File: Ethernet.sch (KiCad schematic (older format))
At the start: 31 parts, among them J1 Wuerth_7499010121A, U3 DP83848C, Y3 25MHz

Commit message: Fix footprints
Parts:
- U3: footprint Package_QFP:LQFP-48_7x7mm_P0.5mm -> Package_QFP:LQFP-48-1EP_7x7mm_P0.5mm_EP3.6x3.6mm
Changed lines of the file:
@@
 F 0 "U3" H 7750 4550 50  0000 C CNN
 F 1 "DP83848C" H 7800 4400 50  0000 C CNN
-F 2 "Package_QFP:LQFP-48_7x7mm_P0.5mm" H 9200 1250 50  0001 C CIN
+F 2 "Package_QFP:LQFP-48-1EP_7x7mm_P0.5mm_EP3.6x3.6mm" H 9200 1250 50  0001 C CIN
 F 3 "http://www.ti.com/lit/ds/symlink/dp83848c.pdf" H 8200 2800 50  0001 C CNN
 	1    8200 2800

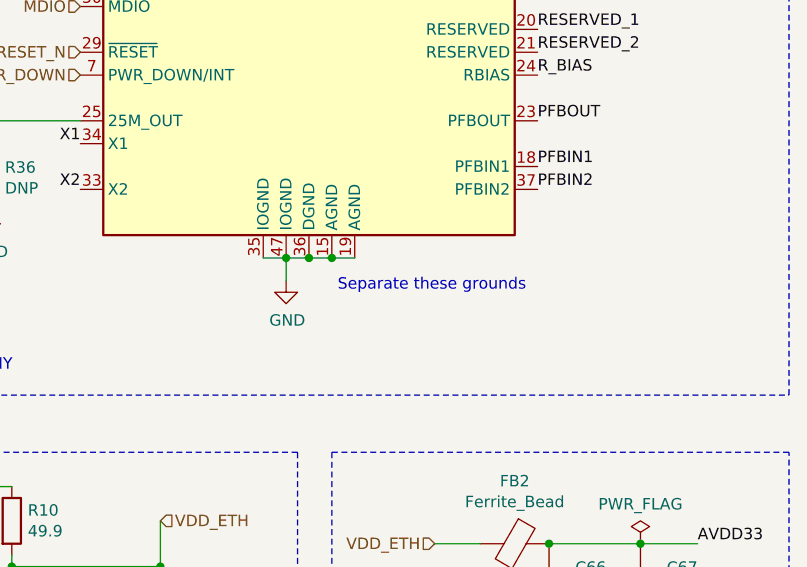
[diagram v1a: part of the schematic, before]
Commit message: Add mounting holes
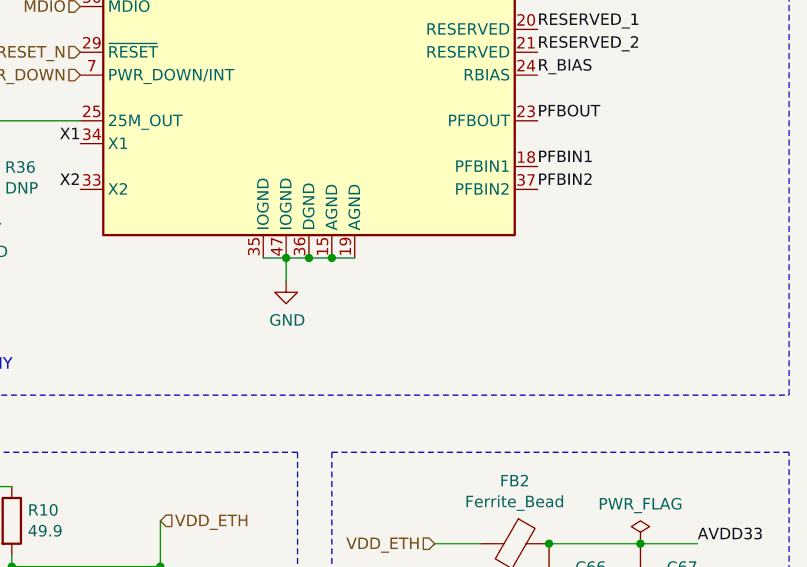
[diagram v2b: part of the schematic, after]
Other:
- note removed: "Separate these grounds\n"
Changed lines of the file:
@@
 	1    0    0    -1
 $EndComp
-Text Notes 9150 4550 2    50   ~ 0
-Separate these grounds\n
 $Comp
 L power:GND #PWR019
